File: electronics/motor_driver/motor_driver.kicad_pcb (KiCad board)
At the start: 2 copper layers, 50 x 50 mm, 72 parts, among them J1 Power, J2 Control, J3 Motor, Q1 FDD86381, Q2 FDD86381, Q3 FDD86381, Q4 FDD86381, U1 SY8502, U2 L78L05_SOT89, U3 LTV-356T, U4 TLP2270, U5 L6393, U6 L6393, U7 LTV-356T

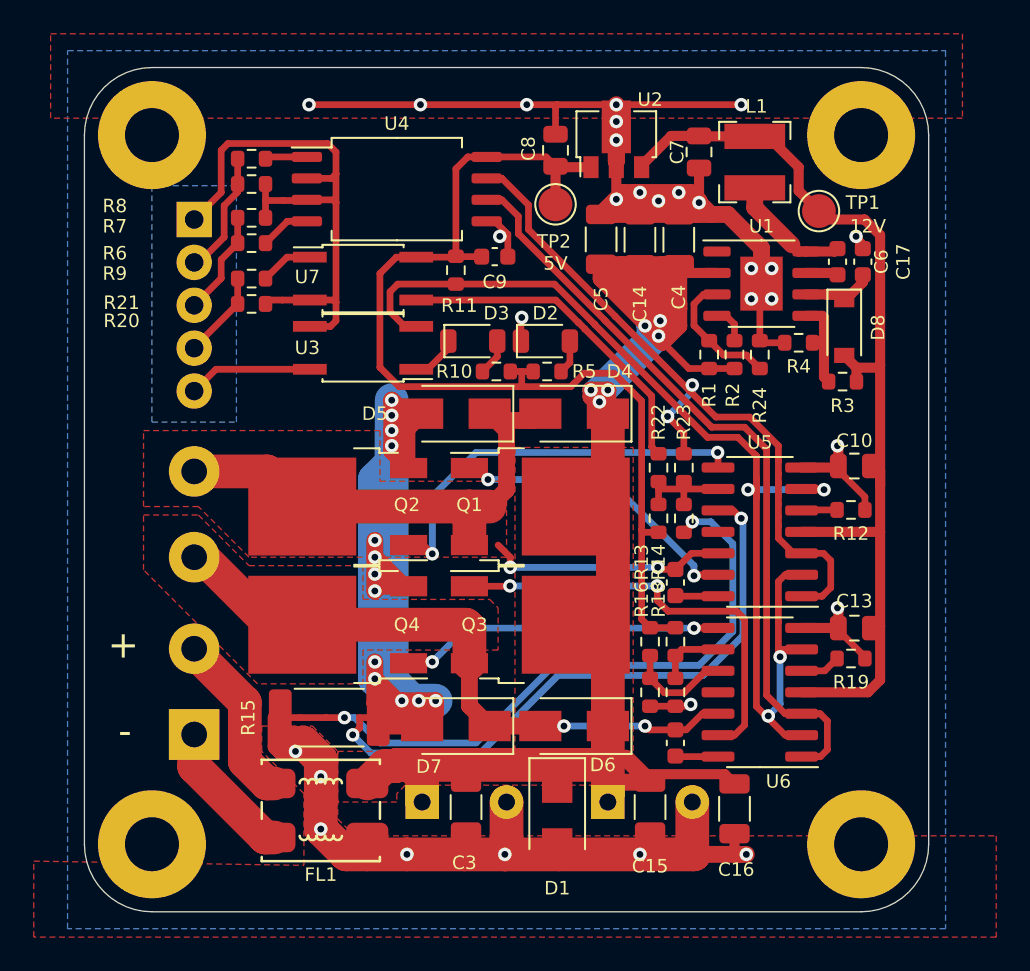
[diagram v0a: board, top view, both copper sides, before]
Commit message: Update motor driver and power control PCB designs
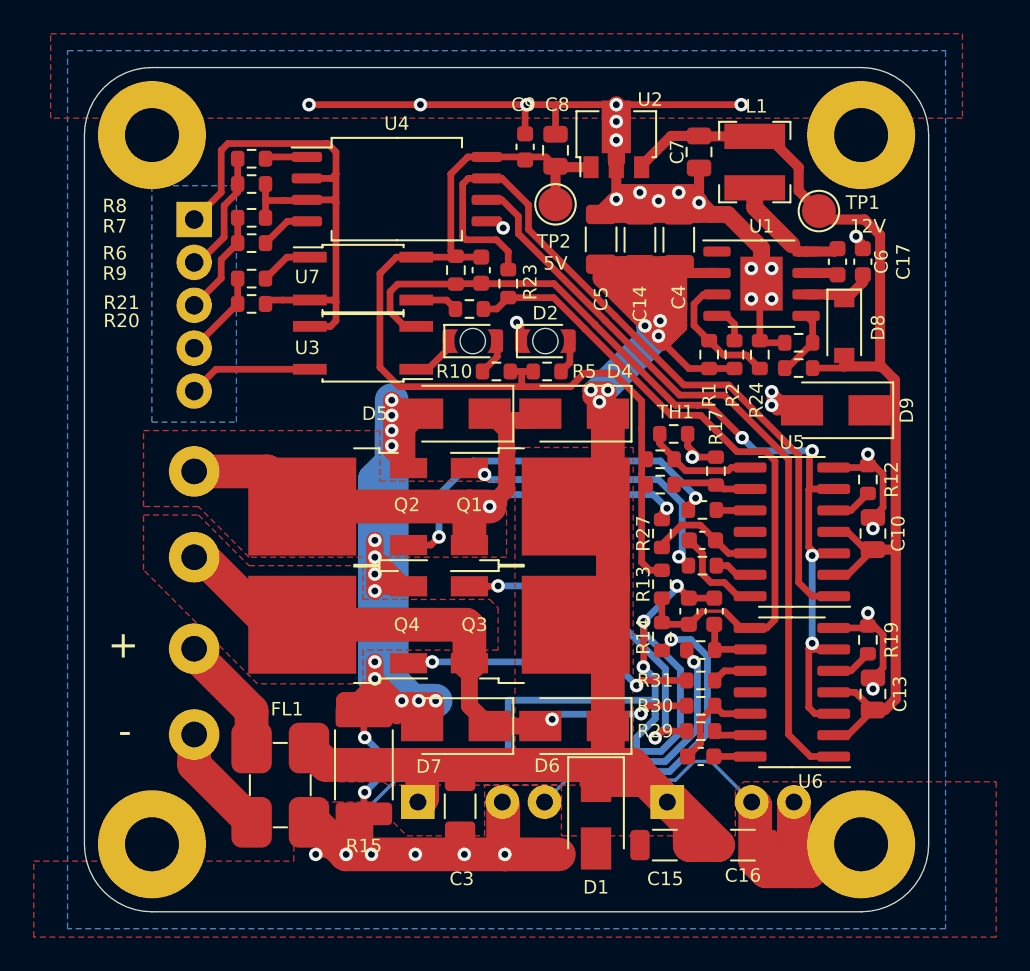
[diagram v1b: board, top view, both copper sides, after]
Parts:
- added C18: 1nF, Capacitor_SMD:C_0603_1608Metric, F.Cu at (78.5, 77.0)
- added C19: 1nF, Capacitor_SMD:C_0603_1608Metric, F.Cu at (92.3, 97.2)
- added C20: 1nF, Capacitor_SMD:C_0603_1608Metric, F.Cu at (90.8, 97.2)
- added D9: SMAJ13A, Diode_SMD:D_SMA, F.Cu at (99.5, 85.3)
- added R25: 1k, Resistor_SMD:R_0603_1608Metric, F.Cu at (91.5, 99.5)
- added R26: 10, Resistor_SMD:R_0603_1608Metric, F.Cu at (91.6, 94.5)
- added R27: 10, Resistor_SMD:R_0603_1608Metric, F.Cu at (89.2, 92.6)
- added R28: 10, Resistor_SMD:R_0603_1608Metric, F.Cu at (91.6, 91.2)
- added R29: 10, Resistor_SMD:R_0603_1608Metric, F.Cu at (91.5, 104.3)
- added R30: 10, Resistor_SMD:R_0603_1608Metric, F.Cu at (91.5, 102.8)
- added R31: 10, Resistor_SMD:R_0603_1608Metric, F.Cu at (91.5, 101.3)
- C1, C2: footprint Capacitor_THT:CP_Radial_D10.0mm_P5.00mm -> motor_driver:CP_Radial_D10.0mm_P5.00mm_P7.50mm
- FL1: value EMI_Filter_CommonMode -> DLW5ATN111; footprint motor_driver:CM7060 -> motor_driver:DLW5ATN111
- R11: value 100k -> 10k
- R13: value 100k -> 47k
- moved TH1 15.3 mm to (89.9, 86.7), turned to 0 degrees
- moved R23 15.1 mm to (80.1, 77.8)
- moved R22 14.6 mm to (77.8, 79.3), turned to 180 degrees
- moved R17 13.7 mm to (92.4, 88.9), turned to -90 degrees
- moved R18 10.8 mm to (89.1, 88.2), turned to 180 degrees
- moved R16 9.32 mm to (89.1, 89.7), turned to 180 degrees
- moved R14 7.12 mm to (89.2, 98.7)
- moved C9 6.74 mm to (81.1, 69.7), turned to 90 degrees
- moved C10 4.15 mm to (101.7, 92.6), turned to 90 degrees
- moved C13 4.05 mm to (101.7, 102.1), turned to 90 degrees
- moved R13 3.91 mm to (89.2, 95.6), turned to -90 degrees
- moved C2 3.52 mm to (89.5, 108.5)
- moved R15 3.47 mm to (71.5, 106.3), turned to -90 degrees
- moved C11 2.97 mm to (91.6, 93.0), turned to 180 degrees
- moved FL1 2.83 mm to (66.6, 107.5), turned to 0 degrees
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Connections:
- net /~FAULT_OUT renamed /~{FAULT_OUT}
- C11 pad 1: /Motor+ -> Net-(C11-Pad1)
- C12 pad 1: /Motor- -> Net-(C12-Pad1)
- R11 pad 2: /~FAULT -> /~{FAULT}
- R13 pad 2: Net-(R13-Pad2) -> /ILIMIT
- R14 pad 2: Net-(R13-Pad2) -> /ILIMIT
- R18 pad 1: Net-(R18-Pad1) -> Net-(U5-Pad8)
- R22 pad 1: Net-(R13-Pad2) -> /ILIMIT
- R23 pad 1: Net-(R13-Pad2) -> /ILIMIT
- TH1 pad 1: Net-(R18-Pad1) -> Net-(U5-Pad8)
- U1 pad 1: Net-(U1-Pad1) -> unconnected-(U1-Pad1)
- U3 pad 2: /~FAULT -> /~{FAULT}
- U5 pad 10: Net-(R15-Pad2) -> Net-(U5-Pad10)
- U5 pad 11: Net-(U5-Pad11) -> unconnected-(U5-Pad11)
- U5 pad 12: /Motor+ -> Net-(C11-Pad1)
- U5 pad 13: Net-(Q1-Pad1) -> Net-(U5-Pad13)
- U5 pad 2: /~FAULT -> +12V
- U5 pad 3: /FWD -> /~{FAULT}
- U5 pad 6: /~FAULT -> /~{FAULT}
- U5 pad 8: Net-(Q2-Pad1) -> Net-(U5-Pad8)
- U5 pad 9: Net-(R13-Pad2) -> Net-(R16-Pad1)
- U6 pad 10: Net-(R16-Pad1) -> Net-(U6-Pad10)
- U6 pad 11: Net-(U6-Pad11) -> unconnected-(U6-Pad11)
- U6 pad 12: /Motor- -> Net-(C12-Pad1)
- U6 pad 13: Net-(Q3-Pad1) -> Net-(U6-Pad13)
- U6 pad 2: /~FAULT -> +12V
- U6 pad 3: /REV -> /~{FAULT}
- U6 pad 6: /~FAULT -> /~{FAULT}
- U6 pad 8: Net-(Q4-Pad1) -> /ILIMIT
- U6 pad 9: Net-(R18-Pad1) -> /ISENSE
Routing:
- net GND: track 144.3 -> 228.4 mm, vias 29 -> 35
- net /~FAULT: track 66.0 -> 0.00 mm, vias 4 -> 0
- net /~{FAULT}: track 0.00 -> 53.9 mm, vias 0 -> 4
- net /ILIMIT: track 0.00 -> 40.1 mm
- net /HCURR: track 19.9 -> 2.54 mm
- net +48V: track 126.1 -> 142.0 mm
- net Net-(R15-Pad2): track 36.2 -> 26.2 mm
- net Net-(R14-Pad1): track 38.0 -> 29.9 mm
- net +12V: track 59.9 -> 67.6 mm
- net Net-(U5-Pad8): track 0.00 -> 6.71 mm
- net Net-(R13-Pad2): track 6.64 -> 0.00 mm
- net Net-(C11-Pad1): track 0.00 -> 6.57 mm
- net Net-(C12-Pad1): track 0.00 -> 5.96 mm
- net Net-(Q3-Pad1): track 25.7 -> 20.0 mm
- net Net-(D5-Pad2): track 81.4 -> 85.7 mm
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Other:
- net class Default removed
- board text added: "FAULT"
- board text added: "JPA 1/2022"
- board text added: "PWR"
- board text removed: "JPA 11/2021"
- board text removed: "PWR FAULT"

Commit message: Update wiring diagram & motor driver part values
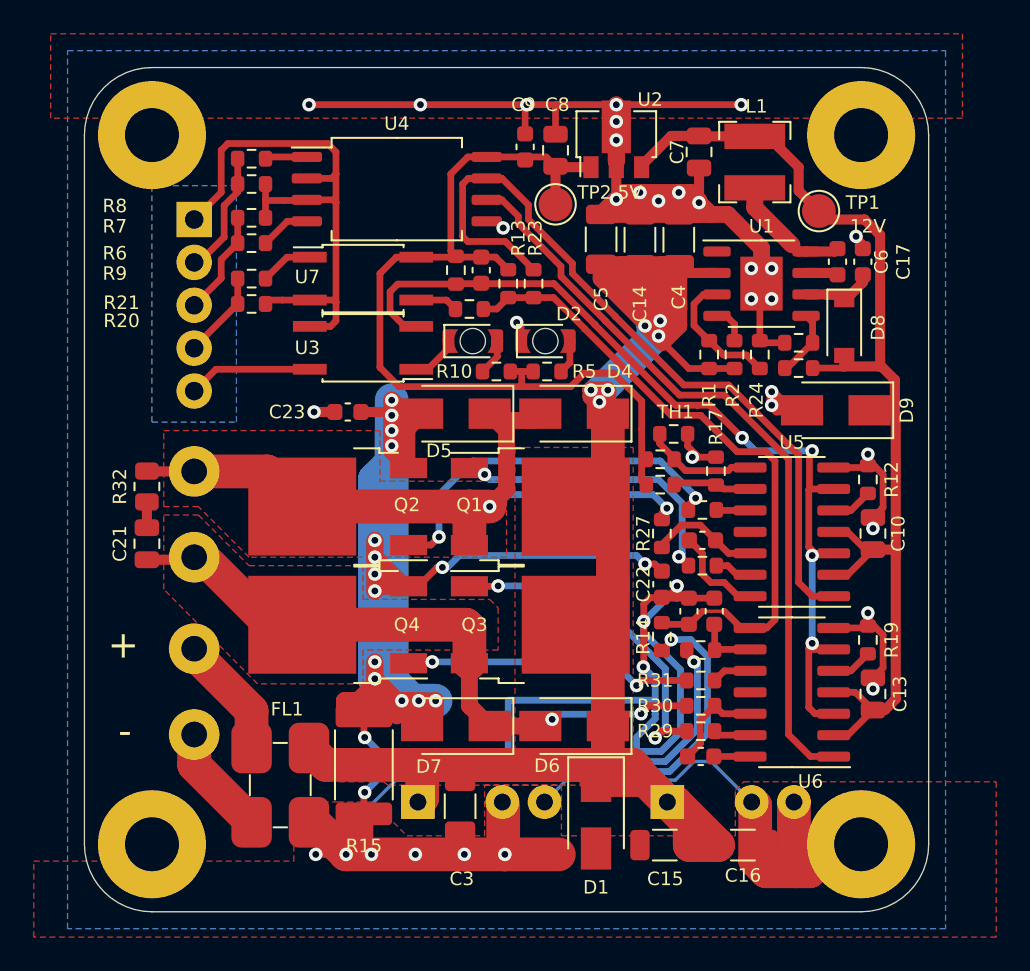
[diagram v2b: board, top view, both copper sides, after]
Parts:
- added C21: 680pF, Capacitor_SMD:C_0805_2012Metric, F.Cu at (58.7, 93.2)
- added C22: 100nF, Capacitor_SMD:C_0603_1608Metric, F.Cu at (89.2, 95.6)
- added C23: 100nF, Capacitor_SMD:C_0603_1608Metric, F.Cu at (70.6, 85.4)
- added R32: 4.7, Resistor_SMD:R_0805_2012Metric, F.Cu at (58.7, 89.8)
- C3, C4: value 1uF/100V -> 1µF/100V
- R12, R19: value 20k -> 47k
- R26, R27, R29, R30: value 10 -> 51
- moved R13 20.0 mm to (80.1, 77.8)
- moved R23 1.50 mm to (81.6, 77.8)
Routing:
- net Net-(D5-Pad2): track 85.7 -> 103.7 mm, vias 13 -> 15
- net GND: track 228.4 -> 235.6 mm, vias 35 -> 36
- net +5V: track 59.3 -> 54.6 mm
- net /Motor-: track 36.5 -> 39.4 mm
- net /Motor+: track 45.7 -> 48.5 mm
- net Net-(C21-Pad1): track 0.00 -> 1.53 mm
- net /ILIMIT: track 40.1 -> 38.6 mm
- net /FWD: track 44.9 -> 45.8 mm
